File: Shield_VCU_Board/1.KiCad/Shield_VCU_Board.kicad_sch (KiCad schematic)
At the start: 164 parts, among them J1 Conn_02x08_Odd_Even, J10 Main_Supply, J11 Conn_01x40_Socket, J12 TFT Wire, J13 Conn_Molex_TouchPanel, J14 CAN_OUT, J15 Conn_01x04_Socket, J2 Conn_02x10_Odd_Even, J3/1 NXP3, J4 Conn_02x08_Odd_Even, J5 Conn_02x10_Odd_Even, J6 Conn_02x10_Odd_Even, J7 Button_Activation_Logic, J8 Conn_ToSpeaker, J9 Wire_x06_Pin, Q1 BSS138, Q2 BSS138, Q3 BSS138, Q4 BSS138, U1 AS1115-BSST, U10 TPS61165-Q1, U11 LM317_SOT-223, U2 SN74LVC1G125DBV, U3 MC74HC14A, U4 TPA6205A1, U5 TLV76133DCY, U6 TLV76150DCY, U7 FT813Q, U8 TLV76133DCY, U9 TLV76133DCY, Y2 SG-210STF

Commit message: NewSupplyArchitecture - v0.1
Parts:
- removed C22, C23: 10uF, Capacitor_Tantalum_SMD:CP_EIA-2012-12_Kemet-R_HandSolder, symbol Device:C_Polarized_Small
- removed C46: 0.1uF, Capacitor_SMD:C_0805_2012Metric_Pad1.18x1.45mm_HandSolder, symbol Device:C_Small
- removed D5, D6: 1N4002, Diode_SMD:D_SOD-123, symbol Diode:1N4002
- removed R57: 660, Resistor_SMD:R_1206_3216Metric_Pad1.30x1.75mm_HandSolder, symbol Device:R_Small
- removed R58: 1.1k, Resistor_SMD:R_1206_3216Metric_Pad1.30x1.75mm_HandSolder, symbol Device:R_Small
- removed U11: LM317_SOT-223, Package_TO_SOT_SMD:SOT-223-3_TabPin2, symbol Regulator_Linear:LM317_SOT-223
- added C45, C49, C50, C54: 0.1uF, Capacitor_SMD:C_0805_2012Metric_Pad1.18x1.45mm_HandSolder, symbol Device:C_Small
- added C47, C55: 10uF, Capacitor_SMD:C_1210_3225Metric_Pad1.33x2.70mm_HandSolder, symbol Device:C_Small
- added C48, C51, C52, C53: 22uF, Capacitor_SMD:C_0805_2012Metric_Pad1.18x1.45mm_HandSolder, symbol Device:C_Small
- added L3, L4: 10uH, Inductor_SMD:L_Pulse_PA4340, symbol Device:L_Small
- added R59: 523k, Resistor_SMD:R_1206_3216Metric_Pad1.30x1.75mm_HandSolder, symbol Device:R_Small
- added R60, R66: 100k, Resistor_SMD:R_1206_3216Metric_Pad1.30x1.75mm_HandSolder, symbol Device:R_Small
- added R65: 787k, Resistor_SMD:R_1206_3216Metric_Pad1.30x1.75mm_HandSolder, symbol Device:R_Small
- added U12, U13: TPS54202DDC, Package_TO_SOT_SMD:SOT-23-6, symbol Regulator_Switching:TPS54202DDC
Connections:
- net GND: now also C47.2, C48.2, C49.2, C51.2, C52.2, C53.2, C54.2, C55.2, R60.1, R66.1, U12.1 (GND), U13.1 (GND)
- net +12V renamed BAT+
- net BAT+: now also C47.1, C49.1, C54.1, C55.1, U12.3 (VIN), U13.3 (VIN)
- net +7V renamed +3.7V
- net +3.7V: now also C48.1, C52.1, L3.2, R59.2; no longer C29.1, D8.1 (K), U6.3 (VI)
- new net: R59.1, R60.2, U12.4 (FB)
- new net: C45.1, U12.6 (BOOT)
- new net: C45.2, L3.1, U12.2 (SW)
- new net: C50.2, L4.1, U13.2 (SW)
- new net: R65.1, R66.2, U13.4 (FB)
- new net: C50.1, U13.6 (BOOT)
- new net +5.3V: C29.1, C51.1, C53.1, D8.1 (K), L4.2, R65.2, U6.3 (VI)
- no-connect marks 113 -> 114
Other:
- note added: "10V X7R ceramic"
- note added: "16V X7R ceramic"
- note added: "3.7V"
- note added: "5.3V"
- note added: "Main supply"
- note removed: "Main supply 12V & 7V"
- moved on the sheet: BKLTV5, C29, C30, D15, D8, J10, U6, V12

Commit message: Shifting AUD 3V3 -> 5V0
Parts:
- R53: value 635R -> 1k
- U5: value TLV76133DCY -> TLV76150DCY
- renumbered AUDV3.3 to AUDV5
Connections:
- net +3.7V: no longer C27.1, D7.1 (K), U5.3 (VI)
- net +5.3V: now also C27.1, D7.1 (K), U5.3 (VI)
- net 3V3_AUD renamed 5V_AUD
- net 3V3_SPKR renamed 5V0_SPKR
- no-connect marks 114 -> 115
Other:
- moved on the sheet: AUDV5, C27, C28, C47, C48, C49, C50, C51, C52, C53, C54, C55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

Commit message: Major changes here
*GND planes;
*Supply paths
*Chip crystal removed
*Changes with INT/PD/SCK wiring
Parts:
- removed C14, C15: 27pF, Capacitor_SMD:C_0805_2012Metric_Pad1.18x1.45mm_HandSolder, symbol Device:C_Small
- removed Y2: SG-210STF, Oscillator:Oscillator_SMD_SeikoEpson_SG210-4Pin_2.5x2.0mm, symbol Oscillator:SG-210STF
- added J16: CAN_IN, Connector_JST:JST_XH_B2B-XH-A_1x02_P2.50mm_Vertical, symbol Connector:Conn_01x02_Socket
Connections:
- net FT_PD: now also U3.2 (Y1); no longer R21.2, U3.9 (Y4)
- net FT_T_SCK: now also U3.9 (Y4); no longer U3.2 (Y1)
- net MC_INT: now also INT1.1, R20.2, U7.13 (INT_N); no longer U3.11 (A5)
- net MC_MISO: now also MISO1.1, U7.6 (MISO); no longer U3.4 (Y2)
- net MC_PD: now also R21.2, U3.1 (A1); no longer U3.8 (A4)
- net MC_SPI_SCK: now also U3.8 (A4); no longer U3.1 (A1)
- net at CAN_H1.1, J14.1 (Pin_1), J15.1 (Pin_1): now also J16.1 (Pin_1)
- net at CAN_L1.1, J14.2 (Pin_2), J15.2 (Pin_2): now also J16.2 (Pin_2)
- removed net FT_INT: INT1.1, R20.2, U3.10 (Y5), U7.13 (INT_N)
- removed net FT_MISO: MISO1.1, U3.3 (A2), U7.6 (MISO)
- no-connect marks 115 -> 120
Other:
- moved on the sheet: C35, CAN_H1

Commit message: AUDIO chip footprint corrected
Footprint uploaded from Mouser for exact reference.
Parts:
- added 3V7: 3V7, TestPoint:TestPoint_Pad_D1.0mm, symbol Connector:TestPoint
- added 5V3: 5V3, TestPoint:TestPoint_Pad_D1.0mm, symbol Connector:TestPoint
- added AUD+01: AUD+, TestPoint:TestPoint_Pad_D1.0mm, symbol Connector:TestPoint
- added AUD-01: AUD-, TestPoint:TestPoint_Pad_D1.0mm, symbol Connector:TestPoint
- added R24, R25, R26, R28: 220R, Resistor_SMD:R_1206_3216Metric_Pad1.30x1.75mm_HandSolder, symbol Device:R_Small
- BAT+01: renamed from V12; value TestPoint -> BAT+
- J14, J16, J7, J8: footprint Connector_JST:JST_XH_B2B-XH-A_1x02_P2.50mm_Vertical -> Connector_JST:JST_PH_B2B-PH-K_1x02_P2.00mm_Vertical
- R3, R4, R5: value 220R -> 635R
- U4: footprint Package_SON:SON-8-1EP_3x2mm_P0.5mm_EP1.4x1.6mm -> TPA:TPS73601DRBR
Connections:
- net +3.7V: now also 3V7.1
- net +5.3V: now also 5V3.1
- net LED1_PTD26: now also R24.1; no longer Q1.1 (G), R1.2
- net LED2_PTD29: now also R25.1; no longer Q2.1 (G), R17.2
- net LED3_PTD28: now also R26.1; no longer Q3.1 (G), R18.2
- net LED4_PTD31: now also R28.1; no longer Q4.1 (G), R23.2
- net at J8.1 (Pin_1), R15.1, U4.5 (VO+): now also AUD+01.1
- net at J8.2 (Pin_2), R13.1, U4.8 (VO-): now also AUD-01.1
- new net: Q1.1 (G), R1.2, R24.2
- new net: Q2.1 (G), R17.2, R25.2
- new net: Q3.1 (G), R18.2, R26.2
- new net: Q4.1 (G), R23.2, R28.2
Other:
- note added: "BAT+ -> 3.7V"
- note added: "BAT+ -> 5.3V"
- note removed: "3.7V"
- note removed: "5.3V"
- moved on the sheet: C47, C48, C49, C50, C51, C52, C53, C54, C55, D15, J10, J8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

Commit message: GND planes correction
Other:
- moved on the sheet: C49, C50, C51, C53, C55, D15, J10, L4, R65, R66, U13

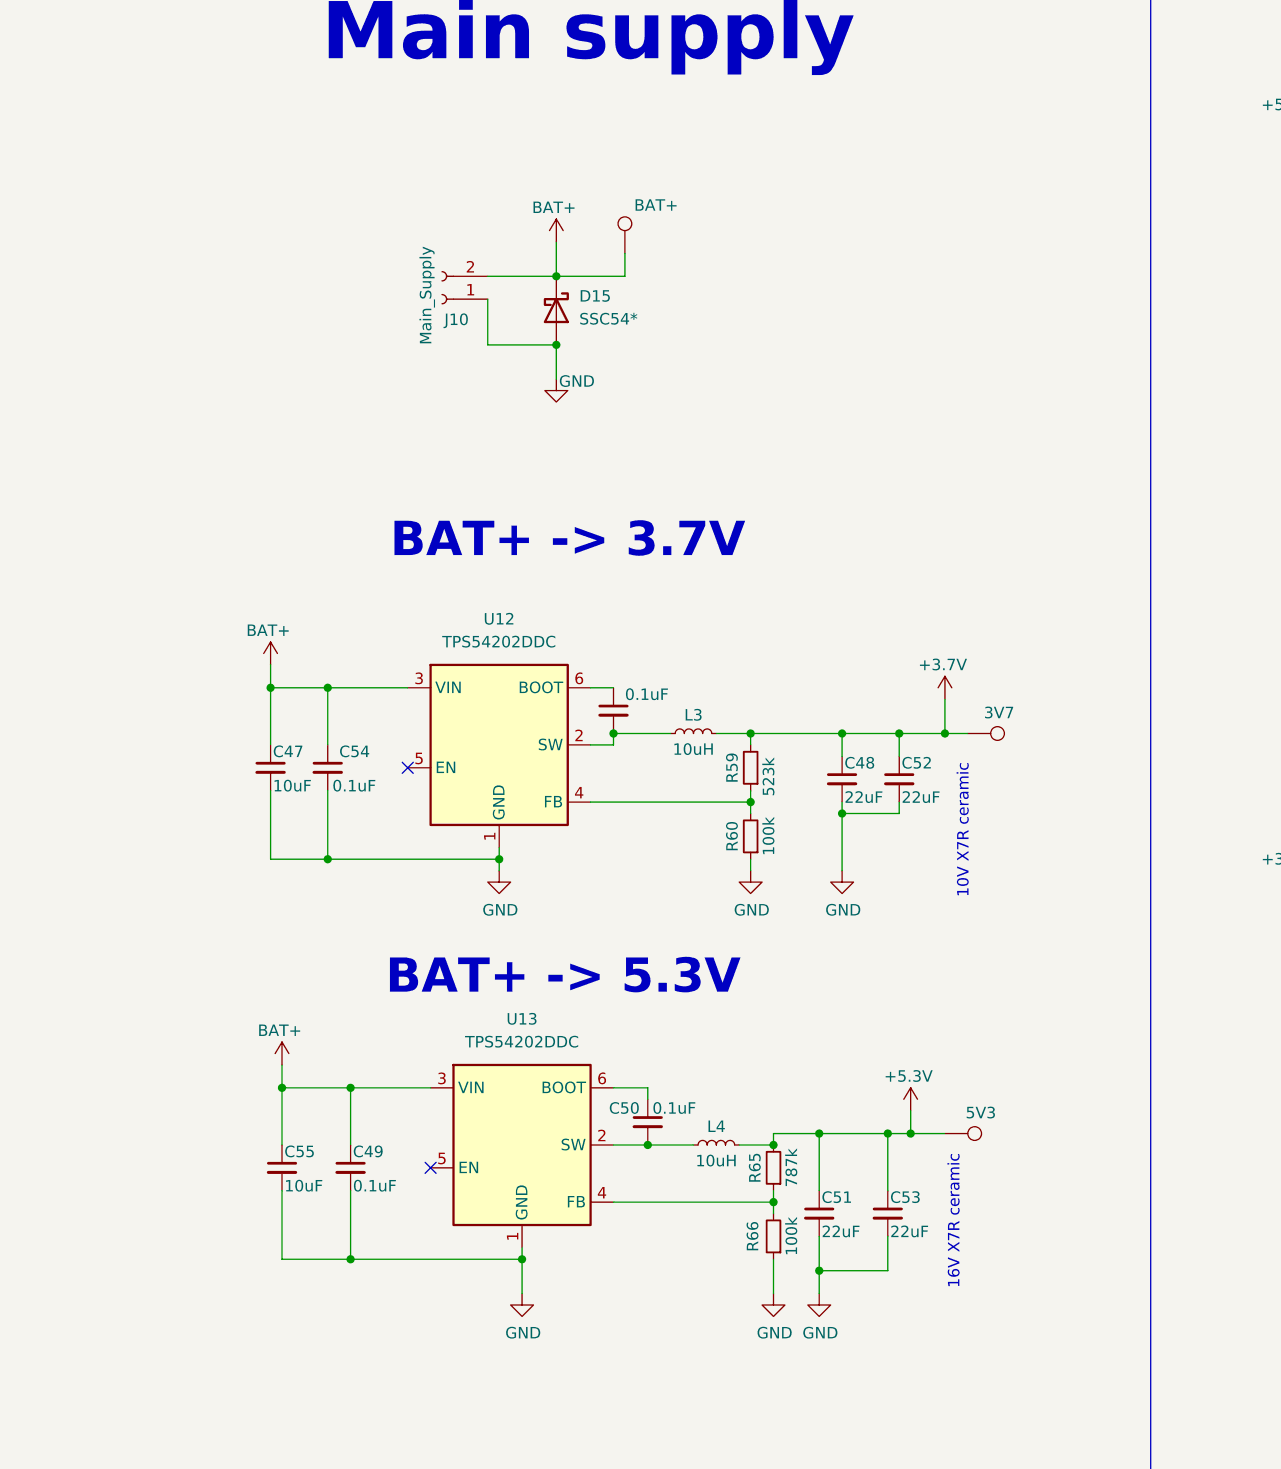
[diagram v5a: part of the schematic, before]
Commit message: DNP 0 Ohm resistors added
DNP resistors added for the case where the Buck converters would have to be bridged.
The DNP resistors are rated by their size: 1206 - 3.0A -> 4.0A that should be more than enough for this Board
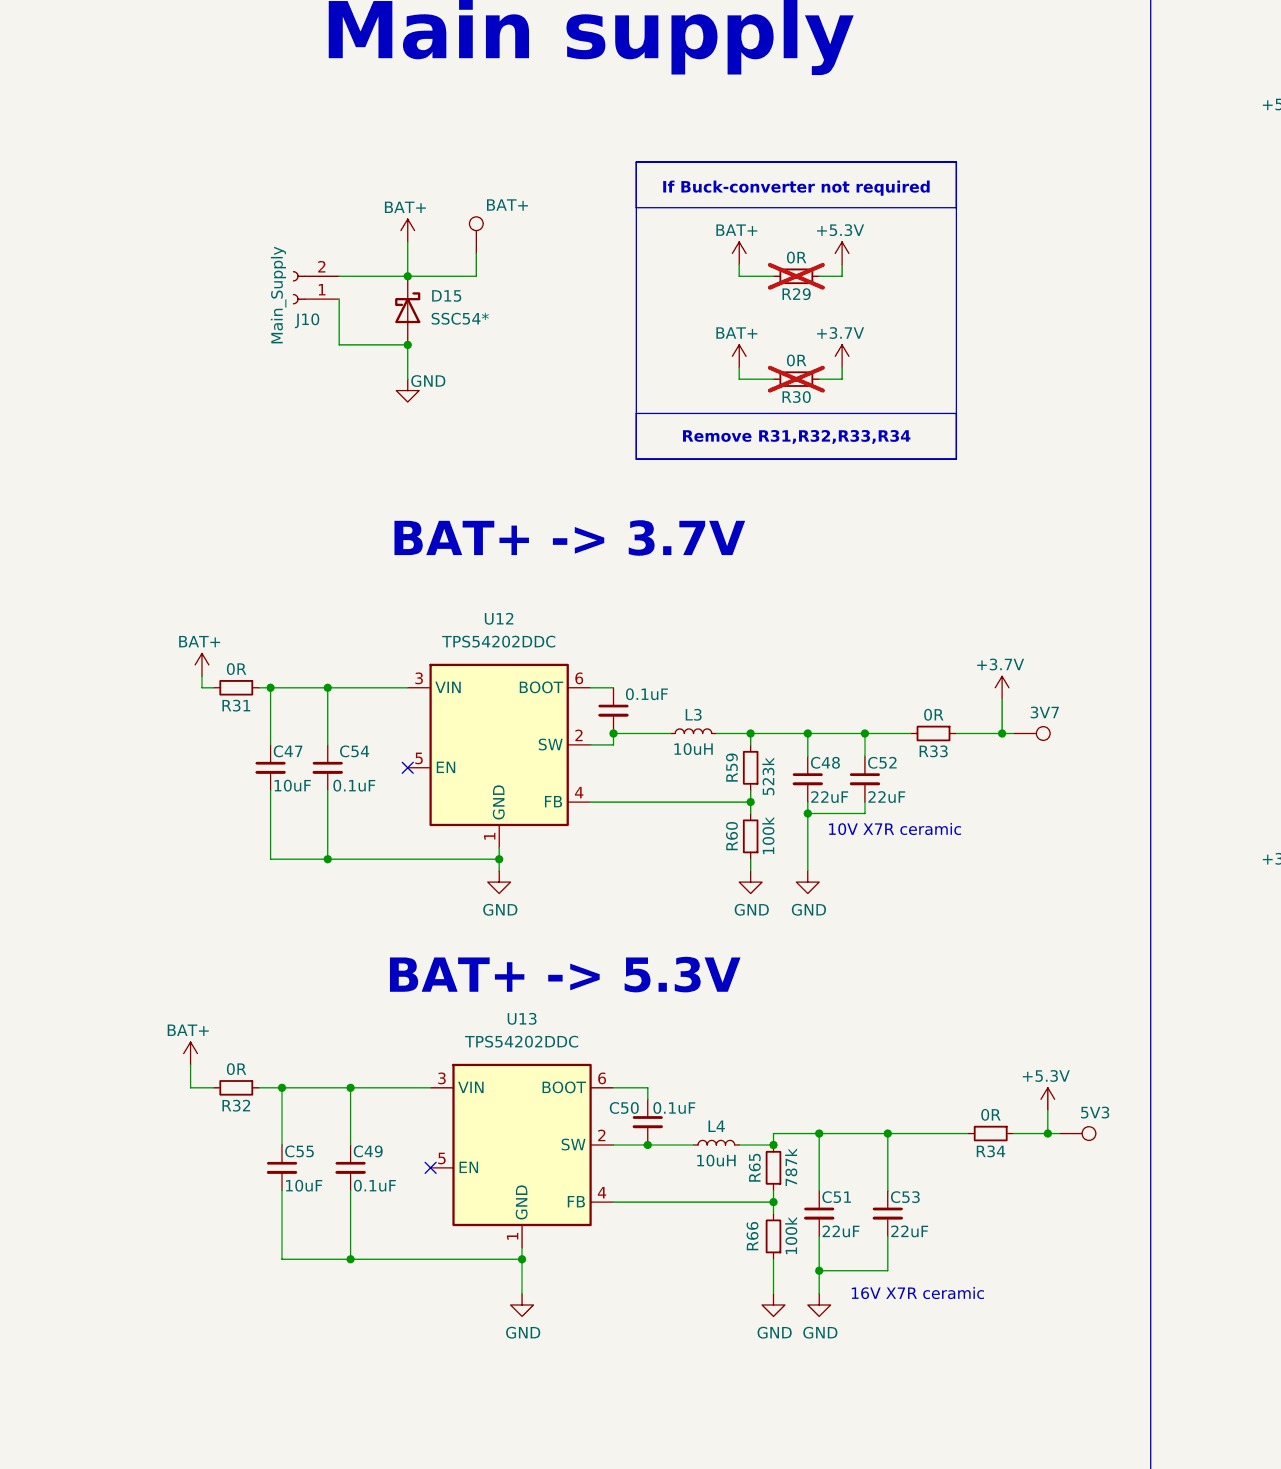
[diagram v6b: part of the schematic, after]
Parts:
- added R29, R30, R31, R32, R33, R34: 0R, Resistor_SMD:R_1206_3216Metric_Pad1.30x1.75mm_HandSolder, symbol Device:R_Small
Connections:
- net +3.7V: now also R30.1, R33.1; no longer C48.1, C52.1, L3.2, R59.2
- net +5.3V: now also R29.1, R34.1; no longer C51.1, C53.1, L4.2, R65.2
- net BAT+: now also R29.2, R30.2, R31.2, R32.2; no longer C47.1, C49.1, C54.1, C55.1, U12.3 (VIN), U13.3 (VIN)
- new net: C48.1, C52.1, L3.2, R33.2, R59.2
- new net: C47.1, C54.1, R31.1, U12.3 (VIN)
- new net: C49.1, C55.1, R32.1, U13.3 (VIN)
- new net: C51.1, C53.1, L4.2, R34.2, R65.2
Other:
- note added: "If Buck-converter not required"
- note added: "Remove R31,R32,R33,R34"
- moved on the sheet: C48, C52, D15, J10

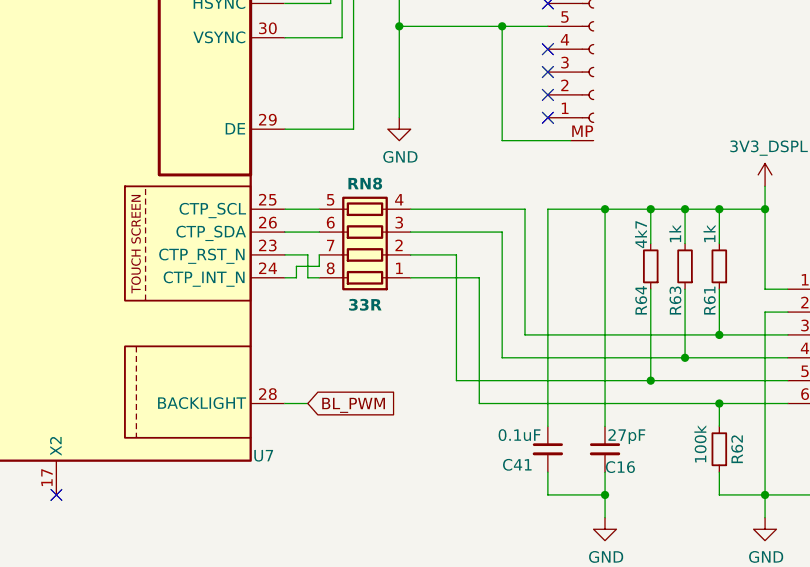
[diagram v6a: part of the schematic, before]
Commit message: Changes to touchscreen i2c and display power
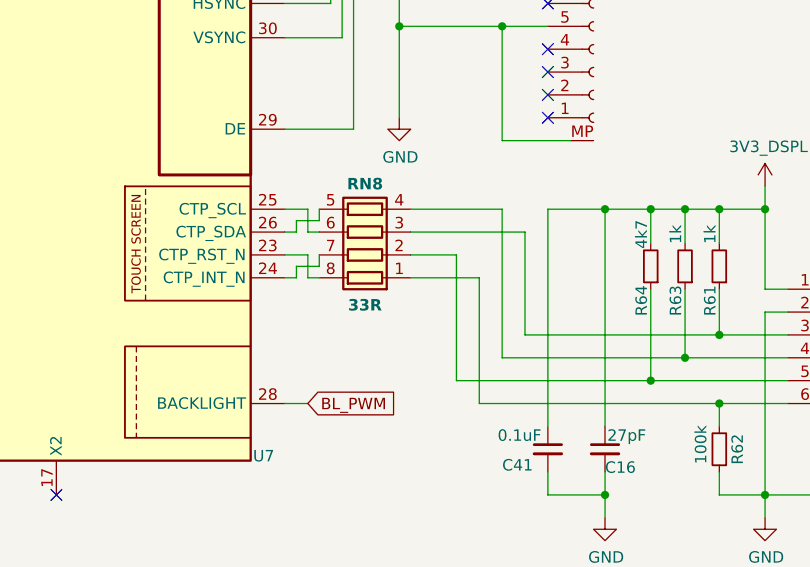
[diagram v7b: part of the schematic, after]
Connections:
- net at J13.3 (Pin_3), R61.1: now also RN8.3 (R3.1); no longer RN8.4 (R4.1)
- net at J13.4 (Pin_4), R63.1: now also RN8.4 (R4.1); no longer RN8.3 (R3.1)
- net at U7.25 (CTP_SCL): now also RN8.6 (R3.2); no longer RN8.5 (R4.2)
- net at U7.26 (CTP_SDA): now also RN8.5 (R4.2); no longer RN8.6 (R3.2)
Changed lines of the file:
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@@
 	(wire
 		(pts
+			(xy 461.01 170.18) (xy 463.55 170.18)
+		)
+		(stroke
+			(width 0)
+			(type default)
+		)
+	)
+	(wire
+		(pts
 			(xy 373.38 198.12) (xy 373.38 196.85)
 		)
@@
 	(wire
 		(pts
-			(xy 473.71 171.45) (xy 483.87 171.45)
-		)
-		(stroke
-			(width 0)
-			(type default)
-		)
-	)
-	(wire
-		(pts
 			(xy 424.18 78.74) (xy 471.17 78.74)
 		)
@@
 	(wire
 		(pts
-			(xy 459.74 168.91) (xy 463.55 168.91)
-		)
-		(stroke
-			(width 0)
-			(type default)
-		)
-	)
-	(wire
-		(pts
 			(xy 58.42 363.22) (xy 58.42 370.84)
 		)
@@
 	(wire
 		(pts
-			(xy 538.48 353.06) (xy 538.48 360.68)
+			(xy 462.28 168.91) (xy 462.28 171.45)
 		)
 		(stroke
@@
 	(wire
 		(pts
-			(xy 513.08 168.91) (xy 513.08 166.37)
+			(xy 538.48 353.06) (xy 538.48 360.68)
 		)
 		(stroke
@@
 	(wire
 		(pts
-			(xy 471.17 78.74) (xy 471.17 82.55)
+			(xy 513.08 168.91) (xy 513.08 166.37)
 		)
 		(stroke
@@
 	(wire
 		(pts
-			(xy 162.56 283.21) (xy 175.26 283.21)
+			(xy 471.17 78.74) (xy 471.17 82.55)
 		)
 		(stroke
@@
 	(wire
 		(pts
-			(xy 69.85 110.49) (xy 55.88 110.49)
+			(xy 162.56 283.21) (xy 175.26 283.21)
 		)
 		(stroke
@@
 	(wire
 		(pts
-			(xy 519.43 49.53) (xy 538.48 49.53)
+			(xy 69.85 110.49) (xy 55.88 110.49)
 		)
 		(stroke
@@
 	(wire
 		(pts
-			(xy 436.88 85.09) (xy 464.82 85.09)
+			(xy 519.43 49.53) (xy 538.48 49.53)
 		)
 		(stroke
@@
 	(wire
 		(pts
-			(xy 459.74 171.45) (xy 463.55 171.45)
+			(xy 436.88 85.09) (xy 464.82 85.09)
 		)
 		(stroke
@@
 	(wire
 		(pts
+			(xy 459.74 168.91) (xy 462.28 168.91)
+		)
+		(stroke
+			(width 0)
+			(type default)
+		)
+	)
+	(wire
+		(pts
 			(xy 519.43 34.29) (xy 528.32 34.29)
 		)
@@
 	(wire
 		(pts
+			(xy 462.28 171.45) (xy 463.55 171.45)
+		)
+		(stroke
+			(width 0)
+			(type default)
+		)
+	)
+	(wire
+		(pts
 			(xy 519.43 105.41) (xy 538.48 105.41)
 		)
@@
 	(wire
 		(pts
-			(xy 486.41 168.91) (xy 486.41 182.88)
-		)
-		(stroke
-			(width 0)
-			(type default)
-		)
-	)
-	(wire
-		(pts
 			(xy 468.63 81.28) (xy 468.63 87.63)
 		)
@@
 	(wire
 		(pts
+			(xy 483.87 168.91) (xy 473.71 168.91)
+		)
+		(stroke
+			(width 0)
+			(type default)
+		)
+	)
+	(wire
+		(pts
 			(xy 411.48 91.44) (xy 411.48 69.85)
 		)
@@
 	(wire
 		(pts
+			(xy 459.74 171.45) (xy 461.01 171.45)
+		)
+		(stroke
+			(width 0)
+			(type default)
+		)
+	)
+	(wire
+		(pts
 			(xy 307.34 78.74) (xy 320.04 78.74)
 		)
@@
 	(wire
 		(pts
+			(xy 461.01 171.45) (xy 461.01 170.18)
+		)
+		(stroke
+			(width 0)
+			(type default)
+		)
+	)
+	(wire
+		(pts
 			(xy 246.38 340.36) (xy 246.38 341.63)
 		)
@@
 	(wire
 		(pts
+			(xy 473.71 171.45) (xy 486.41 171.45)
+		)
+		(stroke
+			(width 0)
+			(type default)
+		)
+	)
+	(wire
+		(pts
 			(xy 60.96 196.85) (xy 68.58 196.85)
 		)
@@
 	(wire
 		(pts
-			(xy 473.71 168.91) (xy 486.41 168.91)
-		)
-		(stroke
-			(width 0)
-			(type default)
-		)
-	)
-	(wire
-		(pts
 			(xy 508 198.12) (xy 508 200.66)
 		)
@@
 	(wire
 		(pts
+			(xy 463.55 168.91) (xy 463.55 170.18)
+		)
+		(stroke
+			(width 0)
+			(type default)
+		)
+	)
+	(wire
+		(pts
 			(xy 378.46 116.84) (xy 396.24 116.84)
 		)
@@
 	(wire
 		(pts
-			(xy 483.87 171.45) (xy 483.87 185.42)
+			(xy 483.87 168.91) (xy 483.87 185.42)
 		)
 		(stroke
@@
 		)
 		(stroke
+			(width 0)
+			(type default)
+		)
+	)
+	(wire
+		(pts
+			(xy 486.41 171.45) (xy 486.41 182.88)
+		)
+		(stroke

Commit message: Check on E-plan
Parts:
- NT1: value 12VTie -> GNDTie
- U4: value TPA6205A1 -> TPA6211A1 - ?
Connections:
- net FT_T_SCK: now also U3.8 (A4); no longer U3.9 (Y4)
- net MC_SPI_SCK: now also U3.9 (Y4); no longer U3.8 (A4)
- no-connect marks 120 -> 121
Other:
- moved on the sheet: AUDV5, BKLTV5, C17, C18, C19, C20, C27, C28, C29, C30, C31, C32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
